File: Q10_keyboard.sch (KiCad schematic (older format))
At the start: 31 parts, among them J1 Conn_01x04, J2 Conn_01x04, J3 Conn_01x04, P1 USB_C_Plug_USB2.0, Q1 BSS138, SW1 SW_SPDT, U1 STM32F103C8Tx, U2 SRV05-4, U3 MIC5219-3.3YM5, U4 BBQ10KBD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

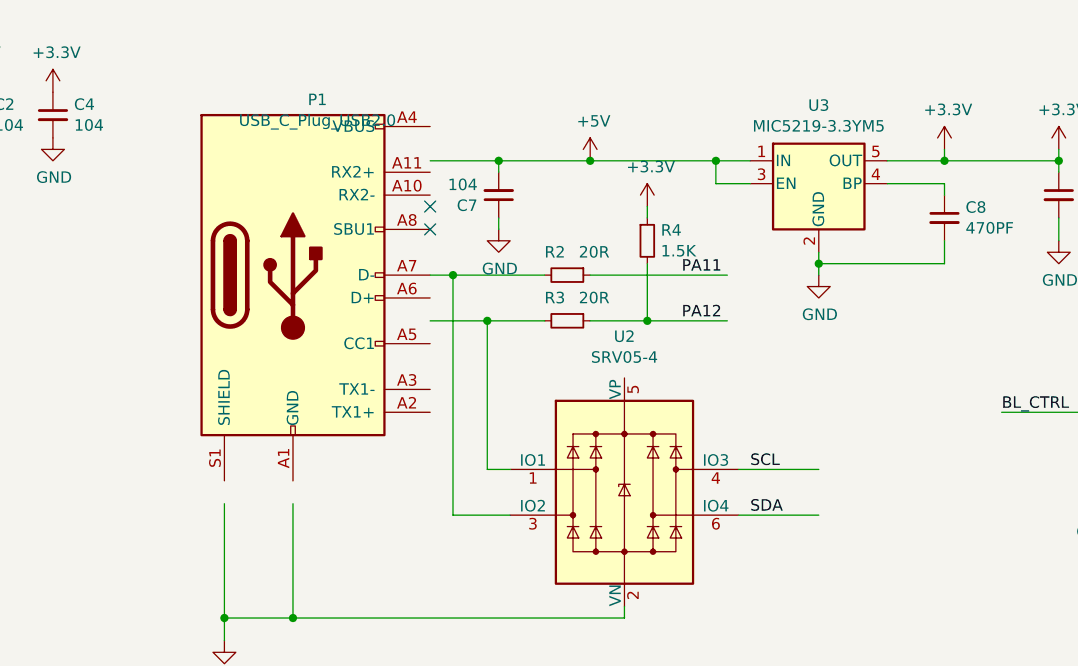
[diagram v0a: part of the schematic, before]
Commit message: Add 5.1k pull-down on USB Type-C CC1 pin
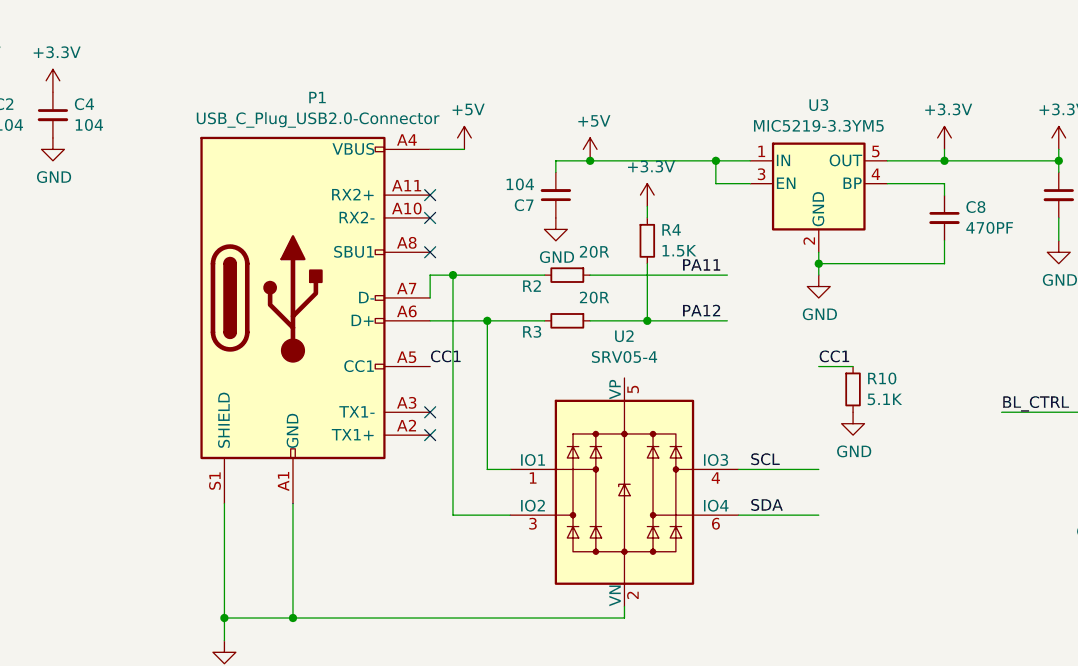
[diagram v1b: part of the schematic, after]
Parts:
- added R10: 5.1K, Resistor_SMD:R_0603_1608Metric_Pad1.05x0.95mm_HandSolder, symbol Q10_keyboard-rescue:R_Small-Device
- P1: value USB_C_Plug_USB2.0 -> USB_C_Plug_USB2.0-Connector; footprint Connector_USB:USB_C_Receptacle_HRO_TYPE-C-31-M-12 -> Q10_keyboard:USB_C_Receptacle_HRO_TYPE-C-31-M-12
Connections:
- net labels added: CC1
- wire segments 163 -> 164
- no-connect marks 2 -> 5
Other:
- moved on the sheet: C7
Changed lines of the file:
@@
 U 1 1 5EF631AD
 P 5650 1950
-F 0 "R3" V 5550 1850 50  0000 L CNN
+F 0 "R3" V 5700 1750 50  0000 L CNN
 F 1 "20R" V 5550 2000 50  0000 L CNN
 F 2 "Resistor_SMD:R_0603_1608Metric_Pad1.05x0.95mm_HandSolder" H 5650 1950 50  0001 C CNN
@@
 U 1 1 5EF64763
 P 5650 1750
-F 0 "R2" V 5550 1650 50  0000 L CNN
+F 0 "R2" V 5700 1550 50  0000 L CNN
 F 1 "20R" V 5550 1800 50  0000 L CNN
 F 2 "Resistor_SMD:R_0603_1608Metric_Pad1.05x0.95mm_HandSolder" H 5650 1750 50  0001 C CNN
@@
 Connection ~ 6750 1700
 Wire Wire Line
-	5050 1250 5350 1250
-Wire Wire Line
 	6450 1350 6300 1350
 Wire Wire Line
@@
 	1    0    0    -1
 $EndComp
-$Comp
-L Q10_keyboard-rescue:USB_C_Plug_USB2.0-Connector P1
-U 1 1 5EFAD10F
-P 4450 1850
-F 0 "P1" H 4557 2717 50  0000 C CNN
-F 1 "USB_C_Plug_USB2.0" H 4557 2626 50  0000 C CNN
-F 2 "Connector_USB:USB_C_Receptacle_HRO_TYPE-C-31-M-12" H 4600 1850 50  0001 C CNN
-F 3 "https://www.usb.org/sites/default/files/documents/usb_type-c.zip" H 4600 1850 50  0001 C CNN
-	1    4450 1850
-	1    0    0    -1
-$EndComp
 Wire Wire Line
 	5400 2600 5300 2600
@@
 	5300 2600 5300 1950
 Wire Wire Line
-	5300 1950 5050 1950
-Connection ~ 5300 1950
-Wire Wire Line
-	5050 1750 5150 1750
-Wire Wire Line
 	5400 2800 5150 2800
 Wire Wire Line
 	5150 2800 5150 1750
-Connection ~ 5150 1750
 Wire Wire Line
 	5150 1750 5550 1750
@@
 	4150 3350 4150 3250
 Connection ~ 4150 3250
-NoConn ~ 5050 1450
-NoConn ~ 5050 1550
+NoConn ~ 5050 1400
 $Comp
 L power:GND #PWR0113
@@
 L Q10_keyboard-rescue:C_Small-Device C7
 U 1 1 5F2C90F5
-P 5350 1400
-F 0 "C7" H 5442 1446 50  0000 L CNN
-F 1 "104" H 5442 1355 50  0000 L CNN
-F 2 "Capacitor_SMD:C_0603_1608Metric_Pad1.05x0.95mm_HandSolder" H 5350 1400 50  0001 C CNN
-F 3 "~" H 5350 1400 50  0001 C CNN
-	1    5350 1400
+P 5600 1400
+F 0 "C7" H 5692 1446 50  0000 L CNN
+F 1 "104" H 5692 1355 50  0000 L CNN
+F 2 "Capacitor_SMD:C_0603_1608Metric_Pad1.05x0.95mm_HandSolder" H 5600 1400 50  0001 C CNN
+F 3 "~" H 5600 1400 50  0001 C CNN
+	1    5600 1400
 	-1   0    0    1
 $EndComp
@@
 L power:GND #PWR0130
 U 1 1 5F2CBA13
-P 5350 1550
-F 0 "#PWR0130" H 5350 1300 50  0001 C CNN
-F 1 "GND" H 5355 1377 50  0000 C CNN
-F 2 "" H 5350 1550 50  0001 C CNN
-F 3 "" H 5350 1550 50  0001 C CNN
-	1    5350 1550
-	1    0    0    -1
-$EndComp
-Wire Wire Line
-	5350 1250 5350 1300
-Connection ~ 5350 1250
-Wire Wire Line
-	5350 1500 5350 1550
+P 5600 1500
+F 0 "#PWR0130" H 5600 1250 50  0001 C CNN
+F 1 "GND" H 5605 1327 50  0000 C CNN
+F 2 "" H 5600 1500 50  0001 C CNN
+F 3 "" H 5600 1500 50  0001 C CNN
+	1    5600 1500
+	1    0    0    -1
+$EndComp
+Wire Wire Line
+	5600 1250 5600 1300
 Wire Wire Line
 	4950 3900 4950 3850
@@
 	-1   0    0    1
 $EndComp
-Wire Wire Line
-	5350 1250 5750 1250
 $Comp
 L Q10_keyboard-rescue:C_Small-Device C9
@@
 Text Label 900  3100 0    50   ~ 0
 ROW3
+$Comp
+L Q10_keyboard-rescue:R_Small-Device R10
+U 1 1 5F8AAB81
+P 6900 2250
+F 0 "R10" H 6959 2296 50  0000 L CNN
+F 1 "5.1K" H 6959 2205 50  0000 L CNN
+F 2 "Resistor_SMD:R_0603_1608Metric_Pad1.05x0.95mm_HandSolder" H 6900 2250 50  0001 C CNN
+F 3 "~" H 6900 2250 50  0001 C CNN
+	1    6900 2250
+	1    0    0    -1
+$EndComp
+$Comp
+L power:GND #PWR03
+U 1 1 5F8BE9BA
+P 6900 2350
+F 0 "#PWR03" H 6900 2100 50  0001 C CNN
+F 1 "GND" H 6905 2177 50  0000 C CNN
+F 2 "" H 6900 2350 50  0001 C CNN
+F 3 "" H 6900 2350 50  0001 C CNN
+	1    6900 2350
+	1    0    0    -1
+$EndComp
+Wire Wire Line
+	5600 1250 5750 1250
+Wire Wire Line
+	6900 2150 6750 2150
+$Comp
+L power:+5V #PWR0134
+U 1 1 5F922F5C
+P 5200 1200
+F 0 "#PWR0134" H 5200 1050 50  0001 C CNN
+F 1 "+5V" H 5215 1373 50  0000 C CNN
+F 2 "" H 5200 1200 50  0001 C CNN
+F 3 "" H 5200 1200 50  0001 C CNN
+	1    5200 1200
+	1    0    0    -1
+$EndComp
+Connection ~ 5300 1950
+Wire Wire Line
+	5300 1950 5050 1950
+Connection ~ 5150 1750
+Wire Wire Line
+	5050 1750 5150 1750
+Wire Wire Line
+	5050 1750 5050 1850
+Wire Wire Line
+	5050 1200 5200 1200
+$Comp
+L Q10_keyboard-rescue:USB_C_Plug_USB2.0-Connector P1
+U 1 1 5F979CA7
+P 4450 1950
+F 0 "P1" H 4557 2925 50  0000 C CNN
+F 1 "USB_C_Plug_USB2.0-Connector" H 4557 2834 50  0000 C CNN
+F 2 "Q10_keyboard:USB_C_Receptacle_HRO_TYPE-C-31-M-12" H 4600 1950 50  0001 C CNN
+F 3 "" H 4600 1950 50  0001 C CNN
+	1    4450 1950
+	1    0    0    -1
+$EndComp
+Text Label 6750 2150 0    50   ~ 0
+CC1
+Text Label 5050 2150 0    50   ~ 0
+CC1
+NoConn ~ 5050 1500
+NoConn ~ 5050 1650
+NoConn ~ 5050 2350
+NoConn ~ 5050 2450
 $EndSCHEMATC
